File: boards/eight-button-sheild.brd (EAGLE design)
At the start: 53.3 x 63.5 mm, 9 parts, among them J4 ARDUINO_R3_SHIELD, SW1 BUTTON, SW2 BUTTON, SW3 BUTTON, SW4 BUTTON, SW5 BUTTON, SW6 BUTTON, SW7 BUTTON, SW8 BUTTON

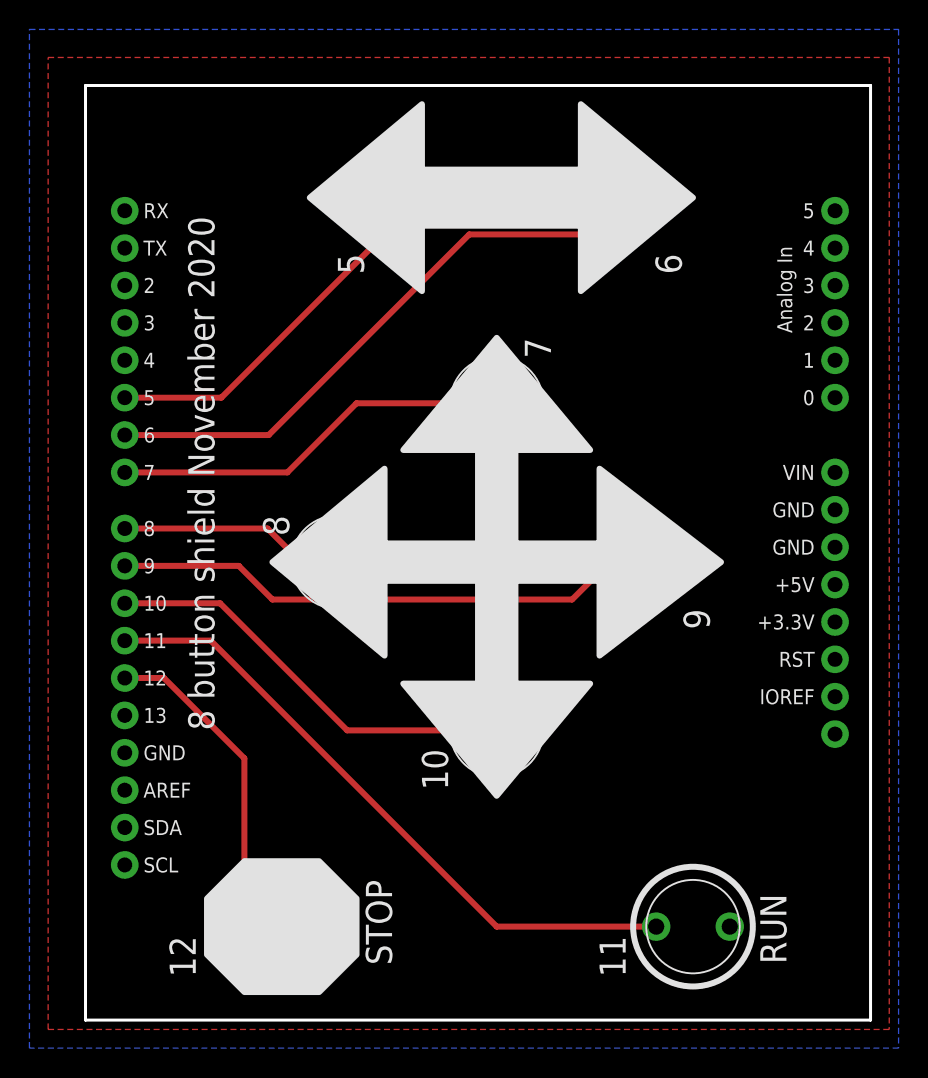
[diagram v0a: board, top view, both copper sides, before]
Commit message: added some breakout plated holes for A0-A6 and power pins to button board
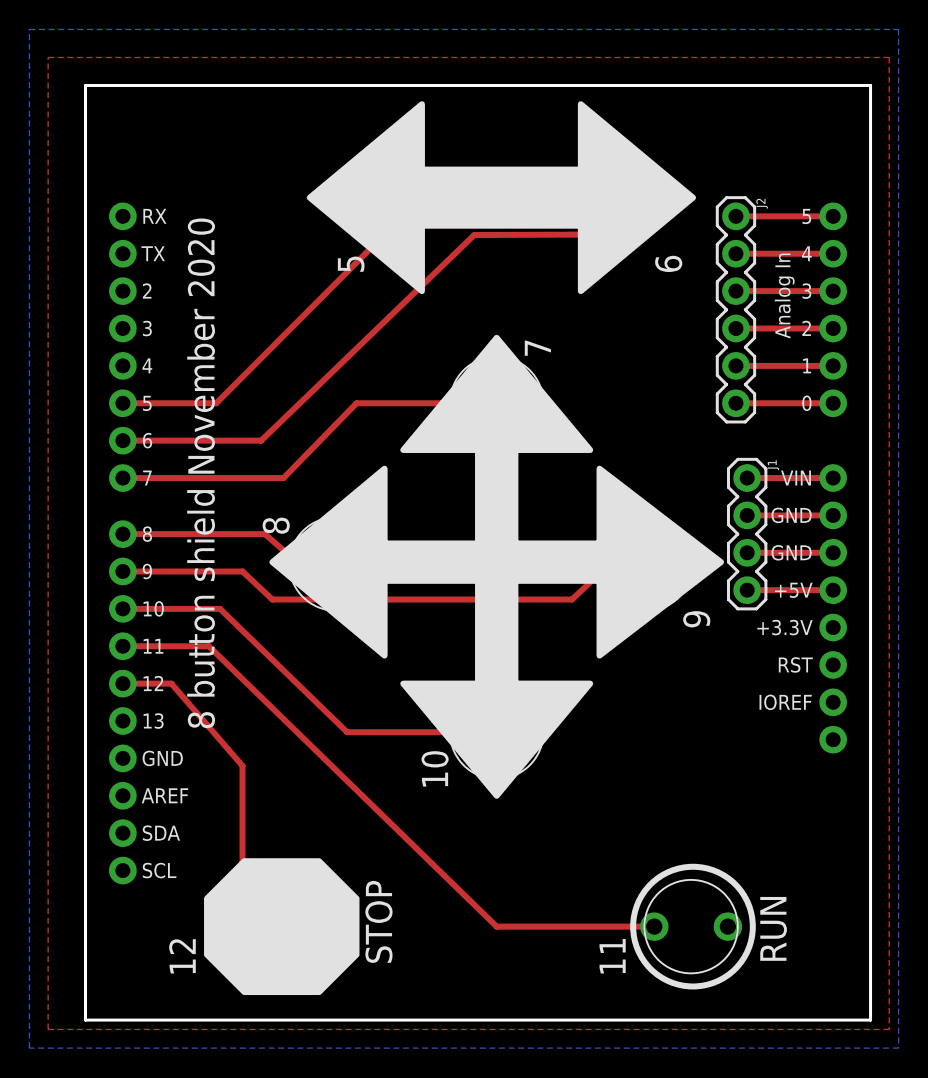
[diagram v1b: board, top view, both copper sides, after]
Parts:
- added J1: (no value), SparkFun-Connectors:1X04
- added J2: (no value), SparkFun-Connectors:1X06
- moved J4 0.40 mm to (0.00, 0.00)
- moved SW4 0.18 mm to (17.0, 31.0)
- moved SW2 0.13 mm to (36.1, 55.9)
- moved SW8 0.13 mm to (13.2, 6.35)
- moved SW5 0.13 mm to (38.1, 31.0)
- moved SW6 0.13 mm to (27.9, 19.6)
- moved SW7 0.13 mm to (41.1, 6.35)
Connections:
- new net N$12: J2.2, J4.A4
- new net N$13: J2.3, J4.A3
- new net N$14: J2.4, J4.A2
- new net N$15: J2.5, J4.A1
- new net N$16: J2.6, J4.A0
- new net N$17: J1.1, J4.VIN
- new net N$18: J1.4, J4.5V
- new net N$9: J2.1, J4.A5
- net GND: now also J1.2, J1.3
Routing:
- net GND: track 0.00 -> 11.7 mm
- net N$9: track 0.00 -> 6.60 mm
- net N$16: track 0.00 -> 6.60 mm
- net N$15: track 0.00 -> 6.60 mm
- net N$14: track 0.00 -> 6.60 mm
- net N$13: track 0.00 -> 6.60 mm
- net N$12: track 0.00 -> 6.60 mm
- net N$18: track 0.00 -> 5.84 mm
- net N$17: track 0.00 -> 5.84 mm
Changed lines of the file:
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@@
 <setting verticaltext="up"/>
 </settings>
-<grid distance="0.025" unitdist="inch" unit="inch" style="lines" multiple="1" display="yes" altdistance="0.05" altunitdist="inch" altunit="inch"/>
+<grid distance="0.01" unitdist="inch" unit="inch" style="lines" multiple="1" display="yes" altdistance="0.05" altunitdist="inch" altunit="inch"/>
 <layers>
 <layer number="1" name="Top" color="4" fill="1" visible="yes" active="yes"/>
@@
 </autorouter>
 <elements>
-<element name="J4" library="SparkFun-Boards" package="UNO_R3_SHIELD" value="ARDUINO_R3_SHIELD" x="0.127" y="0.381"/>
+<element name="J4" library="SparkFun-Boards" package="UNO_R3_SHIELD" value="ARDUINO_R3_SHIELD" x="0" y="0"/>
 <element name="SW1" library="spietz-library" package="BUTTON" value="BUTTON" x="20.32" y="55.88" rot="R90"/>
-<element name="SW2" library="spietz-library" package="BUTTON" value="BUTTON" x="36.195" y="55.88" rot="R90"/>
+<element name="SW2" library="spietz-library" package="BUTTON" value="BUTTON" x="36.068" y="55.88" rot="R90"/>
 <element name="SW3" library="spietz-library" package="BUTTON" value="BUTTON" x="27.94" y="41.91"/>
-<element name="SW4" library="spietz-library" package="BUTTON" value="BUTTON" x="17.145" y="31.115"/>
-<element name="SW5" library="spietz-library" package="BUTTON" value="BUTTON" x="38.1" y="31.115"/>
-<element name="SW6" library="spietz-library" package="BUTTON" value="BUTTON" x="27.94" y="19.685"/>
-<element name="SW7" library="spietz-library" package="BUTTON" value="BUTTON" x="41.275" y="6.35"/>
-<element name="SW8" library="spietz-library" package="BUTTON" value="BUTTON" x="13.335" y="6.35"/>
+<element name="SW4" library="spietz-library" package="BUTTON" value="BUTTON" x="17.018" y="30.988"/>
+<element name="SW5" library="spietz-library" package="BUTTON" value="BUTTON" x="38.1" y="30.988"/>
+<element name="SW6" library="spietz-library" package="BUTTON" value="BUTTON" x="27.94" y="19.558"/>
+<element name="SW7" library="spietz-library" package="BUTTON" value="BUTTON" x="41.148" y="6.35"/>
+<element name="SW8" library="spietz-library" package="BUTTON" value="BUTTON" x="13.208" y="6.35"/>
+<element name="J1" library="SparkFun-Connectors" package="1X04" value="" x="44.958" y="36.83" rot="R270">
+<attribute name="PROD_ID" value="CONN-09696" x="44.958" y="36.83" size="1.778" layer="27" rot="R270" display="off"/>
+</element>
+<element name="J2" library="SparkFun-Connectors" package="1X06" value="" x="44.196" y="54.61" rot="R270">
+<attribute name="PROD_ID" value="CONN-08437" x="44.196" y="54.61" size="1.778" layer="27" rot="R270" display="off"/>
+</element>
 </elements>
 <signals>
@@
 <contactref element="J4" pad="GND@0"/>
 <contactref element="J4" pad="GND@2"/>
+<contactref element="J1" pad="2"/>
+<contactref element="J1" pad="3"/>
+<wire x1="50.8" y1="34.29" x2="44.958" y2="34.29" width="0.4064" layer="1"/>
+<wire x1="44.958" y1="31.75" x2="50.8" y2="31.75" width="0.4064" layer="1"/>
 </signal>
 <signal name="N$30">
@@
 <contactref element="J4" pad="D5"/>
 <contactref element="SW1" pad="P$1"/>
-<wire x1="2.667" y1="42.291" x2="9.230359375" y2="42.291" width="0.4064" layer="1"/>
-<wire x1="9.230359375" y1="42.291" x2="20.32" y2="53.380640625" width="0.4064" layer="1"/>
+<wire x1="2.54" y1="41.91" x2="8.89" y2="41.91" width="0.4064" layer="1"/>
+<wire x1="8.89" y1="41.91" x2="20.32" y2="53.380640625" width="0.4064" layer="1"/>
 </signal>
 <signal name="N$4">
 <contactref element="J4" pad="D6"/>
 <contactref element="SW2" pad="P$1"/>
-<wire x1="2.667" y1="39.751" x2="12.446" y2="39.751" width="0.4064" layer="1"/>
-<wire x1="26.075640625" y1="53.380640625" x2="36.195" y2="53.380640625" width="0.4064" layer="1"/>
-<wire x1="12.446" y1="39.751" x2="26.075640625" y2="53.380640625" width="0.4064" layer="1"/>
+<wire x1="2.54" y1="39.37" x2="11.938" y2="39.37" width="0.4064" layer="1"/>
+<wire x1="26.416" y1="53.34" x2="36.068" y2="53.380640625" width="0.4064" layer="1"/>
+<wire x1="11.938" y1="39.37" x2="26.416" y2="53.34" width="0.4064" layer="1"/>
 </signal>
 <signal name="N$5">
 <contactref element="J4" pad="D7"/>
 <contactref element="SW3" pad="P$1"/>
-<wire x1="2.667" y1="37.211" x2="13.716" y2="37.211" width="0.4064" layer="1"/>
-<wire x1="13.716" y1="37.211" x2="18.415" y2="41.91" width="0.4064" layer="1"/>
+<wire x1="2.54" y1="36.83" x2="13.462" y2="36.83" width="0.4064" layer="1"/>
+<wire x1="13.462" y1="36.83" x2="18.415" y2="41.91" width="0.4064" layer="1"/>
 <wire x1="18.415" y1="41.91" x2="25.440640625" y2="41.91" width="0.4064" layer="1"/>
 </signal>
@@
 <contactref element="J4" pad="D8"/>
 <contactref element="SW4" pad="P$1"/>
-<wire x1="2.667" y1="33.401" x2="12.359640625" y2="33.401" width="0.4064" layer="1"/>
-<wire x1="12.359640625" y1="33.401" x2="14.645640625" y2="31.115" width="0.4064" layer="1"/>
+<wire x1="2.54" y1="33.02" x2="12.192" y2="33.02" width="0.4064" layer="1"/>
+<wire x1="12.192" y1="33.02" x2="14.518640625" y2="30.988" width="0.4064" layer="1"/>
 </signal>
 <signal name="N$7">
 <contactref element="J4" pad="D9"/>
 <contactref element="SW5" pad="P$1"/>
-<wire x1="2.667" y1="30.861" x2="10.414" y2="30.861" width="0.4064" layer="1"/>
-<wire x1="10.414" y1="30.861" x2="12.7" y2="28.575" width="0.4064" layer="1"/>
+<wire x1="2.54" y1="30.48" x2="10.668" y2="30.48" width="0.4064" layer="1"/>
+<wire x1="10.668" y1="30.48" x2="12.7" y2="28.575" width="0.4064" layer="1"/>
 <wire x1="12.7" y1="28.575" x2="33.060640625" y2="28.575" width="0.4064" layer="1"/>
-<wire x1="33.060640625" y1="28.575" x2="35.600640625" y2="31.115" width="0.4064" layer="1"/>
+<wire x1="33.060640625" y1="28.575" x2="35.600640625" y2="30.988" width="0.4064" layer="1"/>
 </signal>
 <signal name="N$8">
 <contactref element="J4" pad="D10"/>
 <contactref element="SW6" pad="P$1"/>
-<wire x1="2.667" y1="28.321" x2="9.144" y2="28.321" width="0.4064" layer="1"/>
-<wire x1="9.144" y1="28.321" x2="17.78" y2="19.685" width="0.4064" layer="1"/>
-<wire x1="17.78" y1="19.685" x2="25.440640625" y2="19.685" width="0.4064" layer="1"/>
+<wire x1="2.54" y1="27.94" x2="9.144" y2="27.94" width="0.4064" layer="1"/>
+<wire x1="9.144" y1="27.94" x2="17.78" y2="19.558" width="0.4064" layer="1"/>
+<wire x1="17.78" y1="19.558" x2="25.440640625" y2="19.558" width="0.4064" layer="1"/>
 </signal>
 <signal name="N$10">
 <contactref element="SW7" pad="P$1"/>
 <contactref element="J4" pad="D11"/>
-<wire x1="2.667" y1="25.781" x2="8.509" y2="25.781" width="0.4064" layer="1"/>
-<wire x1="8.509" y1="25.781" x2="27.94" y2="6.35" width="0.4064" layer="1"/>
-<wire x1="27.94" y1="6.35" x2="38.775640625" y2="6.35" width="0.4064" layer="1"/>
+<wire x1="2.54" y1="25.4" x2="8.382" y2="25.4" width="0.4064" layer="1"/>
+<wire x1="8.382" y1="25.4" x2="27.94" y2="6.35" width="0.4064" layer="1"/>
+<wire x1="27.94" y1="6.35" x2="38.648640625" y2="6.35" width="0.4064" layer="1"/>
 </signal>
 <signal name="N$11">
 <contactref element="SW8" pad="P$1"/>
 <contactref element="J4" pad="D12"/>
-<wire x1="2.667" y1="23.241" x2="5.334" y2="23.241" width="0.4064" layer="1"/>
-<wire x1="5.334" y1="23.241" x2="10.795" y2="17.78" width="0.4064" layer="1"/>
-<wire x1="10.795" y1="17.78" x2="10.795" y2="6.390640625" width="0.4064" layer="1"/>
-<wire x1="10.795" y1="6.390640625" x2="10.835640625" y2="6.35" width="0.4064" layer="1"/>
+<wire x1="2.54" y1="22.86" x2="5.842" y2="22.86" width="0.4064" layer="1"/>
+<wire x1="5.842" y1="22.86" x2="10.668" y2="17.272" width="0.4064" layer="1"/>
+<wire x1="10.668" y1="17.272" x2="10.668" y2="6.35" width="0.4064" layer="1"/>
+<wire x1="10.668" y1="6.35" x2="10.708640625" y2="6.35" width="0.4064" layer="1"/>
+</signal>
+<signal name="N$9">
+<contactref element="J4" pad="A5"/>
+<contactref element="J2" pad="1"/>
+<wire x1="44.196" y1="54.61" x2="50.8" y2="54.61" width="0.4064" layer="1"/>
+</signal>
+<signal name="N$12">
+<contactref element="J4" pad="A4"/>
+<contactref element="J2" pad="2"/>
+<wire x1="44.196" y1="52.07" x2="50.8" y2="52.07" width="0.4064" layer="1"/>
+</signal>
+<signal name="N$13">
+<contactref element="J4" pad="A3"/>
+<contactref element="J2" pad="3"/>
+<wire x1="44.196" y1="49.53" x2="50.8" y2="49.53" width="0.4064" layer="1"/>
+</signal>
+<signal name="N$14">
+<contactref element="J4" pad="A2"/>
+<contactref element="J2" pad="4"/>
+<wire x1="44.196" y1="46.99" x2="50.8" y2="46.99" width="0.4064" layer="1"/>
+</signal>
+<signal name="N$15">
+<contactref element="J4" pad="A1"/>
+<contactref element="J2" pad="5"/>
+<wire x1="50.8" y1="44.45" x2="44.196" y2="44.45" width="0.4064" layer="1"/>
+</signal>
+<signal name="N$16">
+<contactref element="J4" pad="A0"/>
+<contactref element="J2" pad="6"/>
+<wire x1="44.196" y1="41.91" x2="50.8" y2="41.91" width="0.4064" layer="1"/>
+</signal>
+<signal name="N$17">
+<contactref element="J4" pad="VIN"/>
+<contactref element="J1" pad="1"/>
+<wire x1="44.958" y1="36.83" x2="50.8" y2="36.83" width="0.4064" layer="1"/>
+</signal>
+<signal name="N$18">
+<contactref element="J4" pad="5V"/>
+<contactref element="J1" pad="4"/>
+<wire x1="50.8" y1="29.21" x2="44.958" y2="29.21" width="0.4064" layer="1"/>
 </signal>
 </signals>
